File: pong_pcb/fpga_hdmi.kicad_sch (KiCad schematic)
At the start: 10 parts, among them J1 685119134923, U1 TPD12S016RKTR

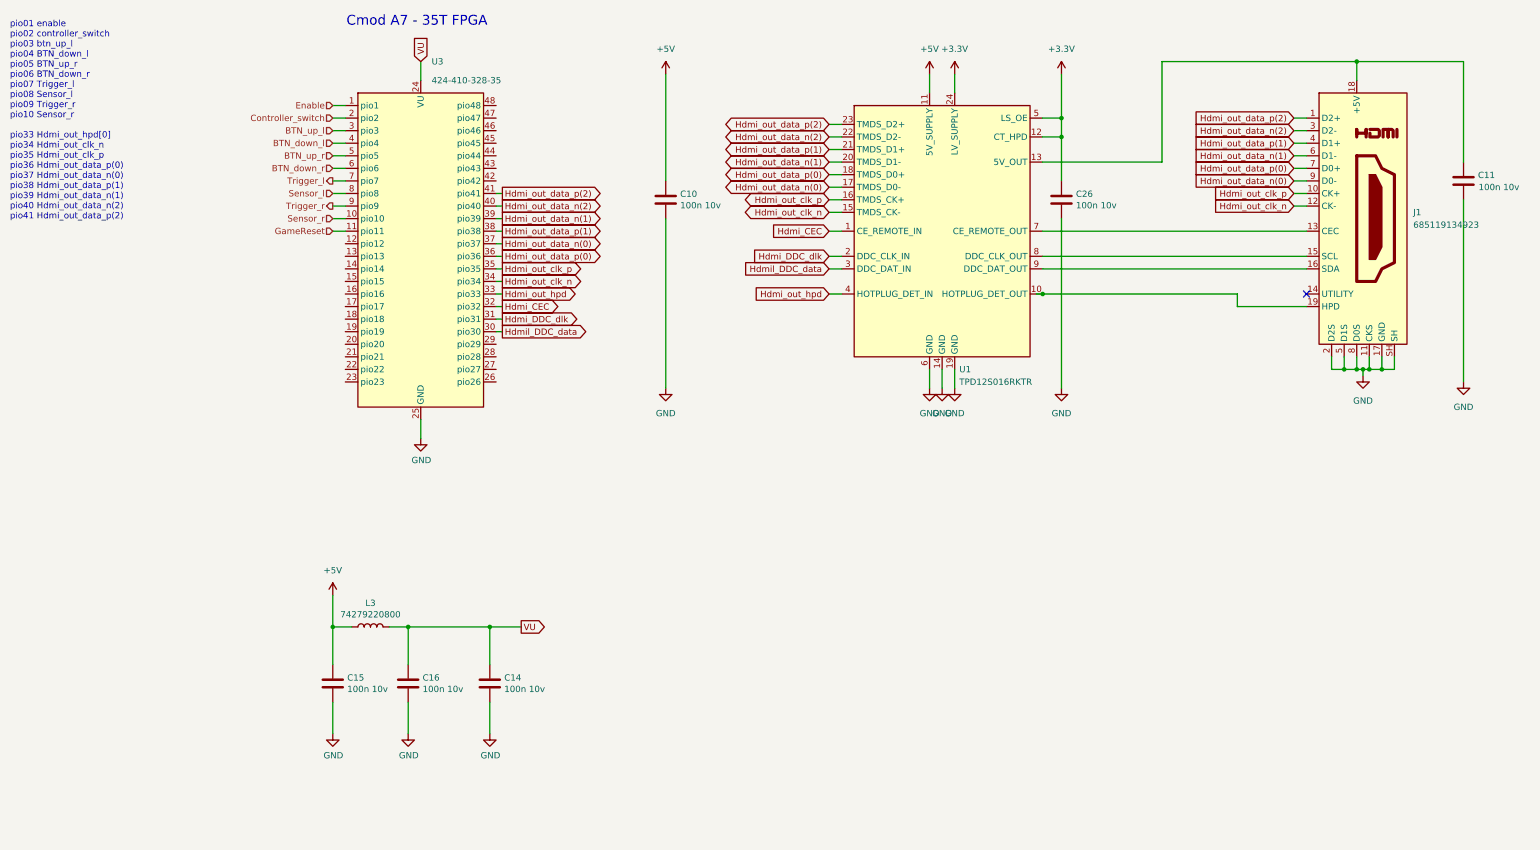
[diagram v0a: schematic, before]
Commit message: Update schema and add packages
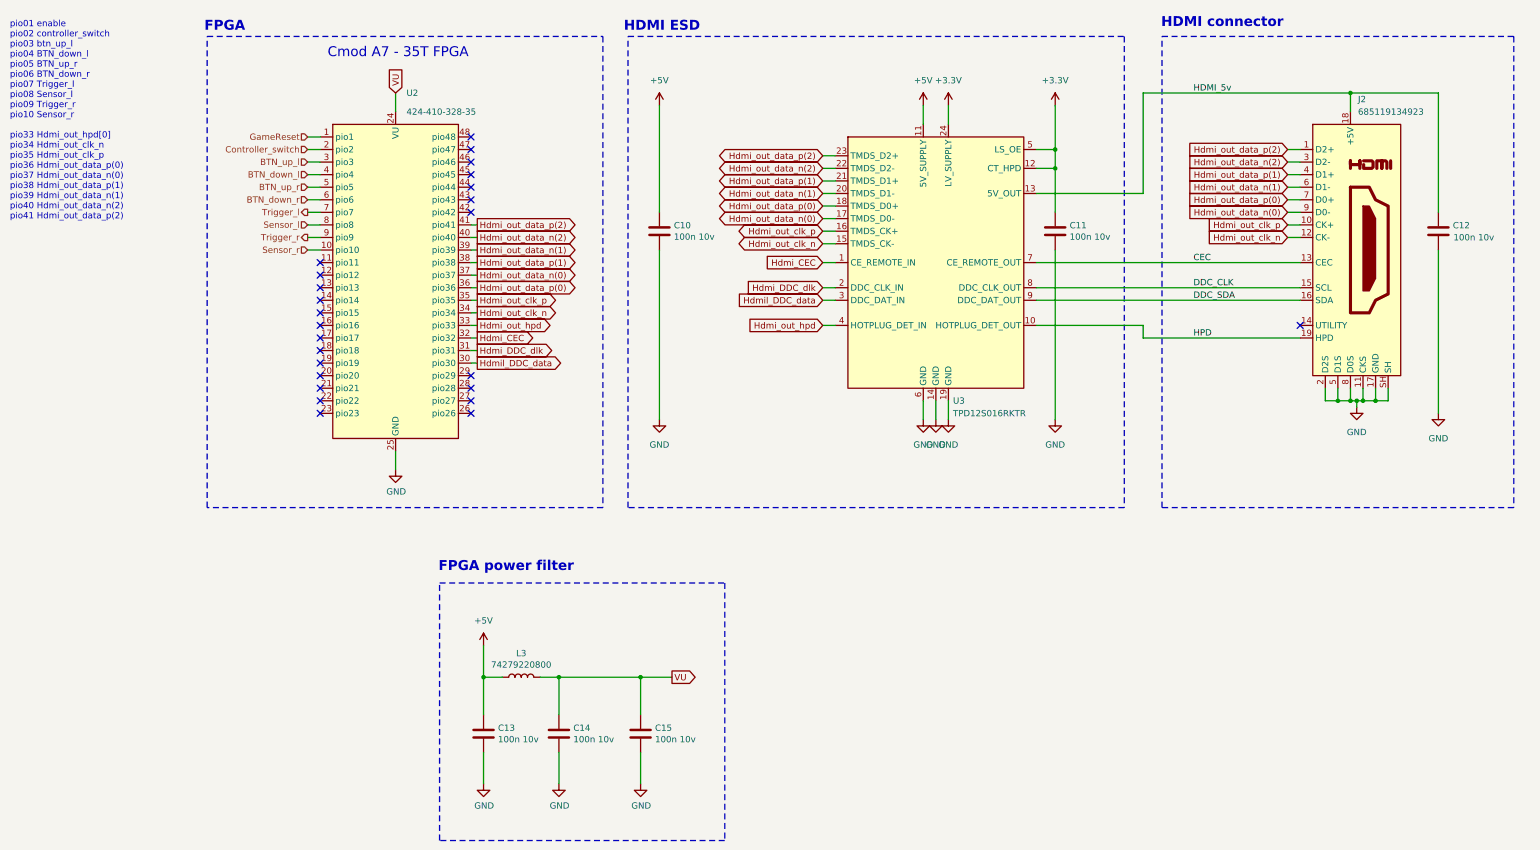
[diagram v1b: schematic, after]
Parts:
- renumbered C26 to C11, C11 to C12, C15 to C13, C16 to C14, C14 to C15, J1 to J2, U3 to U2, U1 to U3
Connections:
- net Enable is gone; now on net GameReset: U2.1 (pio1)
- net GameReset: no longer U2.11 (pio11)
- net HPD: now reaches J2.19 (HPD), U3.10 (HOTPLUG_DET_OUT)
- net HDMI_5v: now reaches C12.1, J2.18 (+5V), U3.13 (5V_OUT)
- net CEC: now reaches J2.13 (CEC), U3.7 (CE_REMOTE_OUT)
- net DDC_CLK: now reaches J2.15 (SCL), U3.8 (DDC_CLK_OUT)
- net DDC_SDA: now reaches J2.16 (SDA), U3.9 (DDC_DAT_OUT)
- no-connect marks 1 -> 25
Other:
- note added: "FPGA"
- note added: "FPGA power filter"
- note added: "HDMI ESD"
- note added: "HDMI connector"
- company: (none) -> Fontys
- title: (none) -> FPGA + HDMI
- moved on the sheet: C10, C11, C12, C13, C14, C15, J2, L3, U2, U3

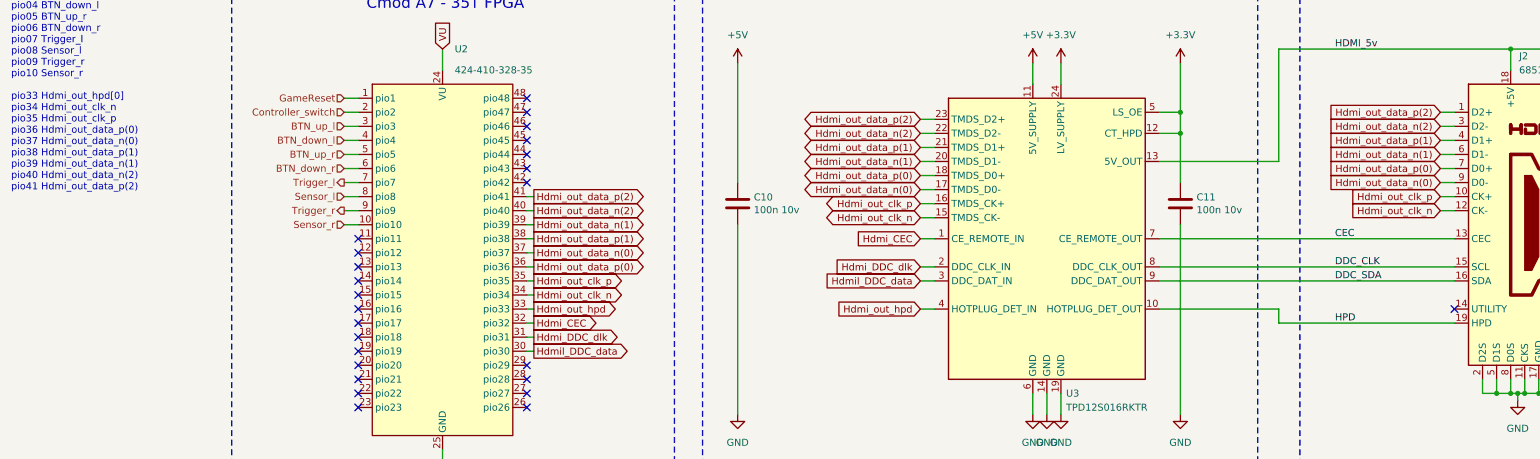
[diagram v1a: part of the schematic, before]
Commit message: Add HDMI layout
And others
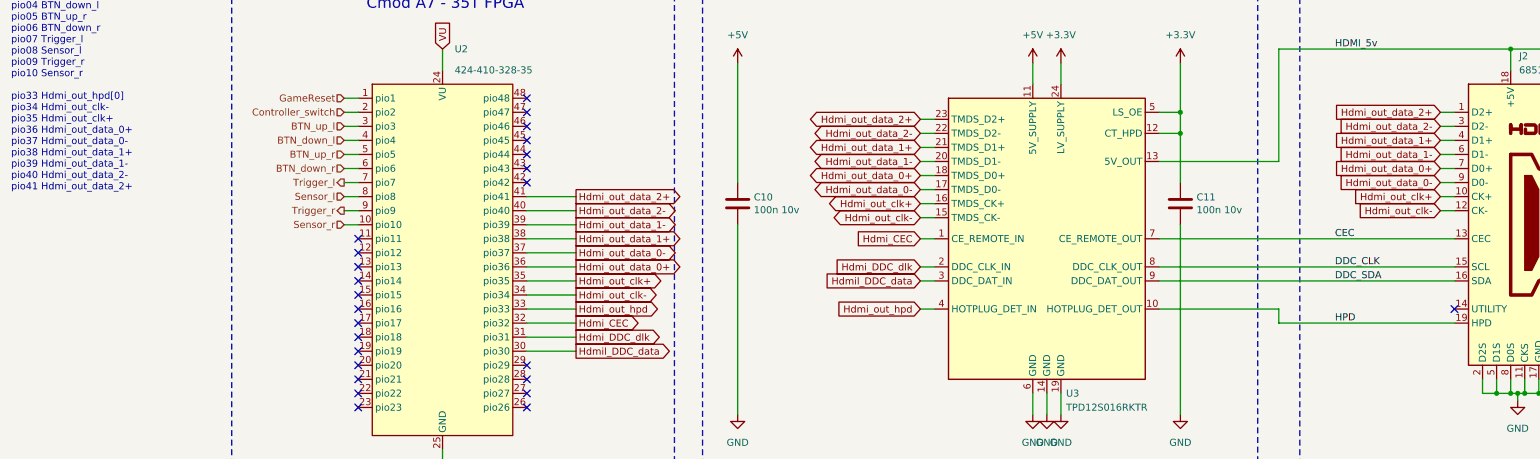
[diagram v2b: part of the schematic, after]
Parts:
- C10, C11, C12, C13, C14, C15: footprint Capacitor_SMD:C_0402_1005Metric_Pad0.74x0.62mm_HandSolder -> Capacitor_SMD:C_0603_1608Metric
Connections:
- net Hdmi_out_clk_n renamed Hdmi_out_clk-
- net Hdmi_out_clk_p renamed Hdmi_out_clk+
- net Hdmi_out_data_n(0) renamed Hdmi_out_data_0-
- net Hdmi_out_data_n(1) renamed Hdmi_out_data_1-
- net Hdmi_out_data_n(2) renamed Hdmi_out_data_2-
- net Hdmi_out_data_p(0) renamed Hdmi_out_data_0+
- net Hdmi_out_data_p(1) renamed Hdmi_out_data_1+
- net Hdmi_out_data_p(2) renamed Hdmi_out_data_2+
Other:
- note added: "pio01 enable pio02 controller_switch pio03 btn_up_l pio04 BTN_down_l pio05 BTN_up_r pio06 BTN_down_r pio07 Trigger_l pio08 Sensor_l pio09 Trigger_r pio10 Sensor_r pio33 Hdmi_out_hpd[0] pio34 Hdmi_out_clk- pio35 Hdmi_out_clk+ pio36 Hdmi_out_data_0+ pio37 Hdmi_out_data_0- pio38 Hdmi_out_data_1+ pio39 Hdmi_out_data_1- pio40 Hdmi_out_data_2- pio41 Hdmi_out_data_2+"
- note removed: "pio01 enable pio02 controller_switch pio03 btn_up_l pio04 BTN_down_l pio05 BTN_up_r pio06 BTN_down_r pio07 Trigger_l pio08 Sensor_l pio09 Trigger_r pio10 Sensor_r pio33 Hdmi_out_hpd[0] pio34 Hdmi_out_clk_n pio35 Hdmi_out_clk_p pio36 Hdmi_out_data_p(0) pio37 Hdmi_out_data_n(0) pio38 Hdmi_out_data_p(1) pio39 Hdmi_out_data_n(1) pio40 Hdmi_out_data_n(2) pio41 Hdmi_out_data_p(2)"

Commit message: Update schema and route PCB
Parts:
- added C13: 47u 10v, Capacitor_SMD:C_1206_3216Metric_Pad1.33x1.80mm_HandSolder, symbol Device:C
- renumbered C13 to C14, C14 to C15, C15 to C16
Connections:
- net +5V: now also C13.1
- net GND: now also C13.2
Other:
- moved on the sheet: C14, C15, C16, L3

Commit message: Other connectors
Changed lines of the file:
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@@
 	(wire
 		(pts
-			(xy 265.43 66.04) (xy 265.43 99.06)
+			(xy 265.43 66.04) (xy 265.43 100.33)
 		)
 		(stroke
@@
 	(wire
 		(pts
-			(xy 248.92 96.52) (xy 248.92 97.79)
+			(xy 248.92 96.52) (xy 248.92 100.33)
 		)
 		(stroke
@@
 	(symbol
 		(lib_id "power:GND")
-		(at 248.92 97.79 0)
+		(at 248.92 100.33 0)
 		(unit 1)
 		(exclude_from_sim no)
@@
 		(fields_autoplaced yes)
 		(property "Reference" "#PWR025"
-			(at 248.92 104.14 0)
+			(at 248.92 106.68 0)
 			(effects
 				(font
@@
 		)
 		(property "Value" "GND"
-			(at 248.92 102.87 0)
+			(at 248.92 105.41 0)
 			(effects
 				(font
@@
 		)
 		(property "Footprint" ""
-			(at 248.92 97.79 0)
+			(at 248.92 100.33 0)
 			(effects
 				(font
@@
 		)
 		(property "Datasheet" ""
-			(at 248.92 97.79 0)
+			(at 248.92 100.33 0)
 			(effects
 				(font
@@
 		)
 		(property "Description" "Power symbol creates a global label with name \"GND\" , ground"
-			(at 248.92 97.79 0)
+			(at 248.92 100.33 0)
 			(effects
 				(font
@@
 	(symbol
 		(lib_id "power:GND")
-		(at 265.43 99.06 0)
+		(at 265.43 100.33 0)
 		(unit 1)
 		(exclude_from_sim no)
@@
 		(fields_autoplaced yes)
 		(property "Reference" "#PWR026"
+			(at 265.43 106.68 0)
+			(effects
+				(font
+					(size 1.27 1.27)
+				)
+				(hide yes)
+			)
+		)
+		(property "Value" "GND"
 			(at 265.43 105.41 0)
 			(effects
@@
 					(size 1.27 1.27)
 				)
-				(hide yes)
-			)
-		)
-		(property "Value" "GND"
-			(at 265.43 104.14 0)
-			(effects
-				(font
-					(size 1.27 1.27)
-				)
 			)
 		)
 		(property "Footprint" ""
-			(at 265.43 99.06 0)
+			(at 265.43 100.33 0)
 			(effects
 				(font
@@
 		)
 		(property "Datasheet" ""
-			(at 265.43 99.06 0)
+			(at 265.43 100.33 0)
 			(effects
 				(font
@@
 		)
 		(property "Description" "Power symbol creates a global label with name \"GND\" , ground"
-			(at 265.43 99.06 0)
-			(effects
-				(font
+			(at 265.43 100.33 0)
+			(effects
+				(font

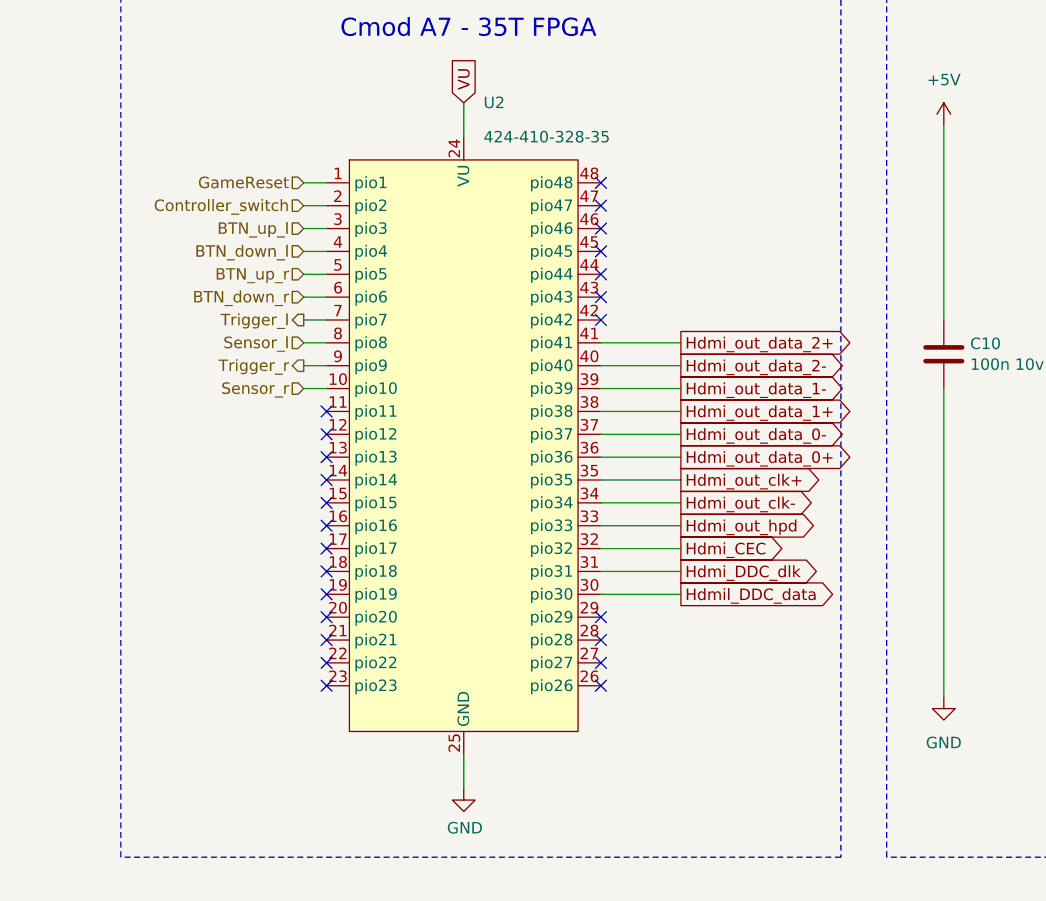
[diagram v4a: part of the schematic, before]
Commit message: Add header pins
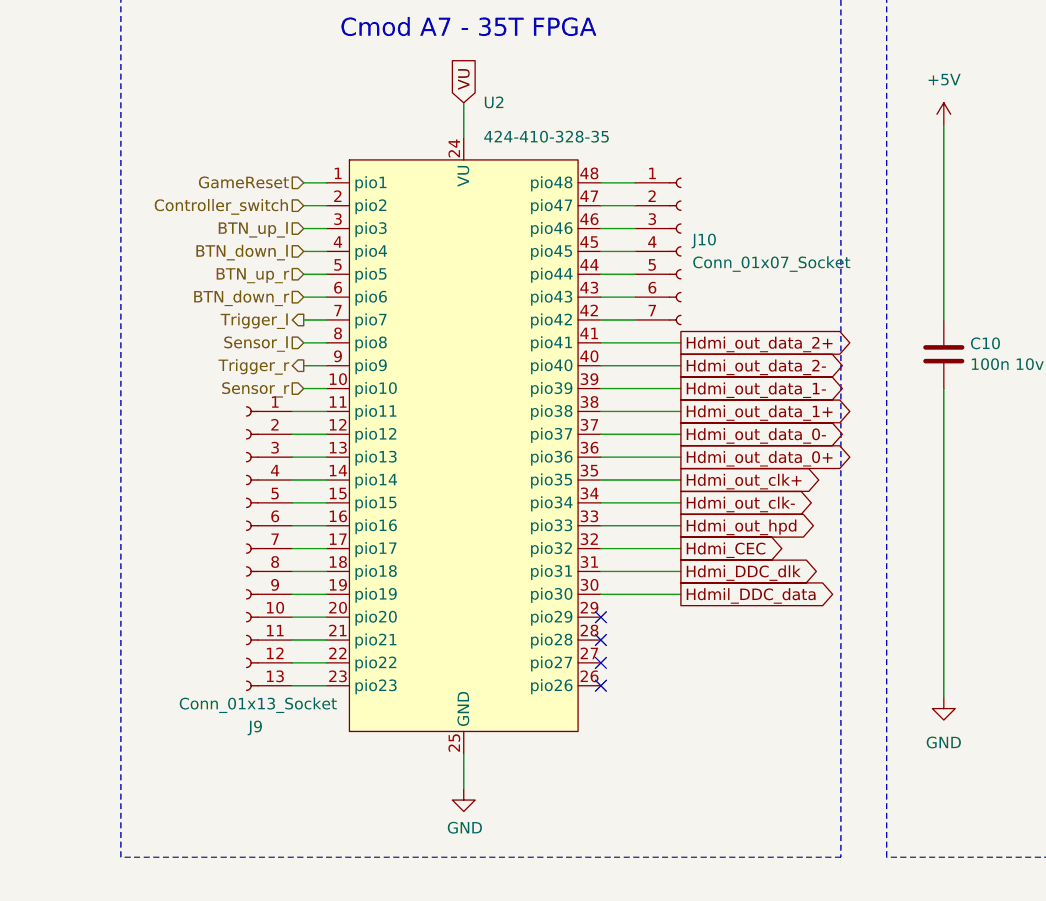
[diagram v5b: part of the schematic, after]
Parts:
- added J10: Conn_01x07_Socket, Connector_PinSocket_2.54mm:PinSocket_2x04_P2.54mm_Vertical, symbol Connector:Conn_01x07_Socket
- added J9: Conn_01x13_Socket, Connector_PinSocket_2.54mm:PinSocket_2x07_P2.54mm_Vertical, symbol Connector:Conn_01x13_Socket
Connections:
- net at U2.11 (pio11): now also J9.1 (Pin_1)
- net at U2.12 (pio12): now also J9.2 (Pin_2)
- net at U2.13 (pio13): now also J9.3 (Pin_3)
- net at U2.14 (pio14): now also J9.4 (Pin_4)
- net at U2.15 (pio15): now also J9.5 (Pin_5)
- net at U2.16 (pio16): now also J9.6 (Pin_6)
- net at U2.17 (pio17): now also J9.7 (Pin_7)
- net at U2.18 (pio18): now also J9.8 (Pin_8)
- net at U2.19 (pio19): now also J9.9 (Pin_9)
- net at U2.20 (pio20): now also J9.10 (Pin_10)
- net at U2.21 (pio21): now also J9.11 (Pin_11)
- net at U2.22 (pio22): now also J9.12 (Pin_12)
- net at U2.23 (pio23): now also J9.13 (Pin_13)
- net at U2.42 (pio42): now also J10.7 (Pin_7)
- net at U2.43 (pio43): now also J10.6 (Pin_6)
- net at U2.44 (pio44): now also J10.5 (Pin_5)
- net at U2.45 (pio45): now also J10.4 (Pin_4)
- net at U2.46 (pio46): now also J10.3 (Pin_3)
- net at U2.47 (pio47): now also J10.2 (Pin_2)
- net at U2.48 (pio48): now also J10.1 (Pin_1)
- no-connect marks 25 -> 5

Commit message: Update TODOs
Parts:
- removed J10: Conn_01x07_Socket, Connector_PinSocket_2.54mm:PinSocket_2x04_P2.54mm_Vertical, symbol Connector:Conn_01x07_Socket
- removed J9: Conn_01x13_Socket, Connector_PinSocket_2.54mm:PinSocket_2x07_P2.54mm_Vertical, symbol Connector:Conn_01x13_Socket
- added J11: Conn_01x08_Socket, Connector_PinSocket_2.54mm:PinSocket_2x04_P2.54mm_Vertical, symbol Connector:Conn_01x08_Socket
- added J9: Conn_01x14_Socket, Connector_PinSocket_2.54mm:PinSocket_2x07_P2.54mm_Vertical, symbol Connector:Conn_01x14_Socket
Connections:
- net GND: now also J11.1 (Pin_1), J9.14 (Pin_14)
- net at U2.48 (pio48): now also J11.2 (Pin_2)
- net at U2.47 (pio47): now also J11.3 (Pin_3)
- net at U2.46 (pio46): now also J11.4 (Pin_4)
- net at U2.45 (pio45): now also J11.5 (Pin_5)
- net at U2.44 (pio44): now also J11.6 (Pin_6)
- net at U2.43 (pio43): now also J11.7 (Pin_7)
- net at U2.42 (pio42): now also J11.8 (Pin_8)
- net at U2.11 (pio11): now also J9.1 (Pin_1)
- net at U2.20 (pio20): now also J9.10 (Pin_10)
- net at U2.21 (pio21): now also J9.11 (Pin_11)
- net at U2.22 (pio22): now also J9.12 (Pin_12)
- net at U2.23 (pio23): now also J9.13 (Pin_13)
- net at U2.12 (pio12): now also J9.2 (Pin_2)
- net at U2.13 (pio13): now also J9.3 (Pin_3)
- net at U2.14 (pio14): now also J9.4 (Pin_4)
- net at U2.15 (pio15): now also J9.5 (Pin_5)
- net at U2.16 (pio16): now also J9.6 (Pin_6)
- net at U2.17 (pio17): now also J9.7 (Pin_7)
- net at U2.18 (pio18): now also J9.8 (Pin_8)
- net at U2.19 (pio19): now also J9.9 (Pin_9)
